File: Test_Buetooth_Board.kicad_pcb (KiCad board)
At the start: 2 copper layers, 100 x 100 mm, 7 parts, among them U1 WH-BLE103a, U2 YM23, U3 HLK-B40, U4 WL6601-TC, U5 E104-BT52, U6 E104-BT01, U7 E104-BT5010A

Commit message: SCH: Se termina la primera versión del sch. PCB: Se ordenan unos componentes
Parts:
- added C1: 100n, 1-Capacitor:C_0805_2012Metric, F.Cu at (130.5, 48.9)
- added C10: 10n, 1-Capacitor:C_0805_2012Metric, F.Cu at (172.6, 57.6)
- added C11: 100n, 1-Capacitor:C_0805_2012Metric, F.Cu at (234.1, 317.2)
- added C12: 10n, 1-Capacitor:C_0805_2012Metric, F.Cu at (234.1, 320.2)
- added C13: 100n, 1-Capacitor:C_0805_2012Metric, F.Cu at (153.2, 184.4)
- added C14: 10n, 1-Capacitor:C_0805_2012Metric, F.Cu at (153.2, 187.4)
- added C15: 100n, 1-Capacitor:C_0805_2012Metric, F.Cu at (153.2, 190.4)
- added C16: 100n, 1-Capacitor:C_0805_2012Metric, F.Cu at (153.2, 193.5)
- added C17: 10n, 1-Capacitor:C_0805_2012Metric, F.Cu at (157.6, 178.4)
- added C18: 100n, 1-Capacitor:C_0805_2012Metric, F.Cu at (157.6, 181.4)
- added C19: 100n, 1-Capacitor:C_0805_2012Metric, F.Cu at (157.6, 184.4)
- added C2: 100n, 1-Capacitor:C_0805_2012Metric, F.Cu at (121.1, 52.6)
- added C20: 10n, 1-Capacitor:C_0805_2012Metric, F.Cu at (157.6, 187.4)
- added C21: 100n, 1-Capacitor:C_0805_2012Metric, F.Cu at (157.6, 190.4)
- added C3: 10n, 1-Capacitor:C_0805_2012Metric, F.Cu at (123.2, 52.6)
- added C4: 100n, 1-Capacitor:C_0805_2012Metric, F.Cu at (103.5, 53.3)
- added C5: 100n, 1-Capacitor:C_0805_2012Metric, F.Cu at (160.4, 54.2)
- added C7: 100n, 1-Capacitor:C_0805_2012Metric, F.Cu at (136.1, 53.8)
- added C8: 10n, 1-Capacitor:C_0805_2012Metric, F.Cu at (138.1, 53.8)
- added C9: 100n, 1-Capacitor:C_0805_2012Metric, F.Cu at (174.7, 57.6)
- added D1: LED, 1-Led:LED_0805, F.Cu at (135.7, 70.2)
- added D2: LED, 1-Led:LED_0805, F.Cu at (127.8, 64.2)
- added D3: LED, 1-Led:LED_0805, F.Cu at (190.4, 65.5)
- added D4: LED, 1-Led:LED_0805, F.Cu at (161.5, 70.3)
- added D5: LED, 1-Led:LED_0805, F.Cu at (194.4, 65.5)
- added D6: LED, 1-Led:LED_0805, F.Cu at (159.2, 169.0)
- added D7: LED, 1-Led:LED_0805, F.Cu at (159.2, 172.0)
- added J1: Screw_Terminal_01x04, Connector_PinHeader_2.54mm:PinHeader_1x04_P2.54mm_Vertical, F.Cu at (101.5, 94.1)
- added J12: Screw_Terminal_01x02, Connector_PinHeader_2.54mm:PinHeader_1x02_P2.54mm_Vertical, F.Cu at (177.3, 77.9)
- added J13: Screw_Terminal_01x02, Connector_PinHeader_2.54mm:PinHeader_1x02_P2.54mm_Vertical, F.Cu at (181.9, 77.9)
- added J14: Screw_Terminal_01x02, Connector_PinHeader_2.54mm:PinHeader_1x02_P2.54mm_Vertical, F.Cu at (186.6, 77.9)
- added J15: Screw_Terminal_01x02, Connector_PinHeader_2.54mm:PinHeader_1x02_P2.54mm_Vertical, F.Cu at (230.7, 296.4)
- added J16: Screw_Terminal_01x05, Connector_PinHeader_2.54mm:PinHeader_1x05_P2.54mm_Vertical, F.Cu at (176.6, 72.3)
- added J17: Screw_Terminal_01x02, Connector_PinHeader_2.54mm:PinHeader_1x02_P2.54mm_Vertical, F.Cu at (202.8, 303.6)
- added J18: Screw_Terminal_01x02, Connector_PinHeader_2.54mm:PinHeader_1x02_P2.54mm_Vertical, F.Cu at (207.4, 303.6)
- added J19: Screw_Terminal_01x02, Connector_PinHeader_2.54mm:PinHeader_1x02_P2.54mm_Vertical, F.Cu at (212.1, 303.6)
- added J20: Screw_Terminal_01x02, Connector_PinHeader_2.54mm:PinHeader_1x02_P2.54mm_Vertical, F.Cu at (135.8, 164.8)
- added J21: Screw_Terminal_01x02, Connector_PinHeader_2.54mm:PinHeader_1x02_P2.54mm_Vertical, F.Cu at (140.5, 164.8)
- added J22: Screw_Terminal_01x02, Connector_PinHeader_2.54mm:PinHeader_1x02_P2.54mm_Vertical, F.Cu at (145.1, 164.8)
- added J23: Screw_Terminal_01x05, Connector_PinHeader_2.54mm:PinHeader_1x05_P2.54mm_Vertical, F.Cu at (153.5, 197.3)
- added J24: Screw_Terminal_01x02, Connector_PinHeader_2.54mm:PinHeader_1x02_P2.54mm_Vertical, F.Cu at (149.8, 164.8)
- added J25: Screw_Terminal_01x02, Connector_PinHeader_2.54mm:PinHeader_1x02_P2.54mm_Vertical, F.Cu at (121.9, 172.0)
- added J26: Screw_Terminal_01x02, Connector_PinHeader_2.54mm:PinHeader_1x02_P2.54mm_Vertical, F.Cu at (126.5, 172.0)
- added J27: Screw_Terminal_01x05, Connector_PinHeader_2.54mm:PinHeader_1x05_P2.54mm_Vertical, F.Cu at (158.1, 197.3)
- added J28: Screw_Terminal_01x06, Connector_PinHeader_2.54mm:PinHeader_1x06_P2.54mm_Vertical, F.Cu at (162.2, 179.2)
- added J29: Screw_Terminal_01x02, Connector_PinHeader_2.54mm:PinHeader_1x02_P2.54mm_Vertical, F.Cu at (131.2, 172.0)
- added J30: Screw_Terminal_01x02, Connector_PinHeader_2.54mm:PinHeader_1x02_P2.54mm_Vertical, F.Cu at (135.8, 172.0)
- added J31: Screw_Terminal_01x02, Connector_PinHeader_2.54mm:PinHeader_1x02_P2.54mm_Vertical, F.Cu at (140.5, 172.0)
- added J32: Screw_Terminal_01x07, 1-Pinhead:PinHeader_1x07_P2.54mm_Vertical, F.Cu at (154.4, 157.6)
- added J33: Screw_Terminal_01x06, Connector_PinHeader_2.54mm:PinHeader_1x06_P2.54mm_Vertical, F.Cu at (141.6, 72.2)
- added J34: Screw_Terminal_01x08, Connector_PinHeader_2.54mm:PinHeader_1x08_P2.54mm_Vertical, F.Cu at (103.5, 69.9)
- added J4: Screw_Terminal_01x02, Connector_PinHeader_2.54mm:PinHeader_1x02_P2.54mm_Vertical, F.Cu at (108.0, 79.0)
- added J5: Screw_Terminal_01x02, Connector_PinHeader_2.54mm:PinHeader_1x02_P2.54mm_Vertical, F.Cu at (112.7, 79.0)
- added J6: Screw_Terminal_01x02, Connector_PinHeader_2.54mm:PinHeader_1x02_P2.54mm_Vertical, F.Cu at (117.3, 79.0)
- added J7: Screw_Terminal_01x02, Connector_PinHeader_2.54mm:PinHeader_1x02_P2.54mm_Vertical, F.Cu at (143.2, 79.1)
- added J8: Screw_Terminal_01x02, Connector_PinHeader_2.54mm:PinHeader_1x02_P2.54mm_Vertical, F.Cu at (147.9, 79.1)
- added J9: Screw_Terminal_01x02, Connector_PinHeader_2.54mm:PinHeader_1x02_P2.54mm_Vertical, F.Cu at (152.6, 79.1)
- added Q1: MMBT3904, Package_TO_SOT_SMD:SOT-23, F.Cu at (127.9, 58.8)
- added Q2: MMBT3904, Package_TO_SOT_SMD:SOT-23, F.Cu at (135.7, 65.1)
- added Q3: MMBT3904, Package_TO_SOT_SMD:SOT-23, F.Cu at (161.6, 65.2)
- added Q4: MMBT3904, Package_TO_SOT_SMD:SOT-23, F.Cu at (190.4, 60.4)
- added Q5: MMBT3904, Package_TO_SOT_SMD:SOT-23, F.Cu at (194.5, 60.4)
- added Q6: MMBT3904, Package_TO_SOT_SMD:SOT-23, F.Cu at (144.1, 197.8)
- added Q7: MMBT3904, Package_TO_SOT_SMD:SOT-23, F.Cu at (144.1, 202.4)
- added R1: 100, 1-Resistor:R_0805_2012Metric, F.Cu at (100.0, 53.3)
- added R10: 10k, 1-Resistor:R_0805_2012Metric, F.Cu at (135.7, 62.1)
- added R11: 2k2, 1-Resistor:R_0805_2012Metric, F.Cu at (135.7, 68.2)
- added R12: 1k, 1-Resistor:R_0805_2012Metric, F.Cu at (161.6, 60.1)
- added R13: 10k, 1-Resistor:R_0805_2012Metric, F.Cu at (161.6, 62.1)
- added R15: 2k2, 1-Resistor:R_0805_2012Metric, F.Cu at (161.5, 68.2)
- added R16: 10k, 1-Resistor:R_0805_2012Metric, F.Cu at (169.9, 54.2)
- added R17: 10k, 1-Resistor:R_0805_2012Metric, F.Cu at (180.4, 62.1)
- added R18: 100, 1-Resistor:R_0805_2012Metric, F.Cu at (126.2, 187.2)
- added R19: 10k, 1-Resistor:R_0805_2012Metric, F.Cu at (182.6, 62.1)
- added R2: 100, 1-Resistor:R_0805_2012Metric, F.Cu at (130.5, 45.3)
- added R20: 1k, 1-Resistor:R_0805_2012Metric, F.Cu at (190.4, 55.4)
- added R21: 10k, 1-Resistor:R_0805_2012Metric, F.Cu at (190.4, 57.4)
- added R22: 2k2, 1-Resistor:R_0805_2012Metric, F.Cu at (190.4, 63.4)
- added R23: 1k, 1-Resistor:R_0805_2012Metric, F.Cu at (194.5, 55.4)
- added R24: 10k, 1-Resistor:R_0805_2012Metric, F.Cu at (194.5, 57.4)
- added R25: 2k2, 1-Resistor:R_0805_2012Metric, F.Cu at (194.5, 63.4)
- added R26: 10k, 1-Resistor:R_0805_2012Metric, F.Cu at (130.6, 187.2)
- added R27: 10k, 1-Resistor:R_0805_2012Metric, F.Cu at (130.6, 190.2)
- added R28: 1k, 1-Resistor:R_0805_2012Metric, F.Cu at (130.6, 193.1)
- added R29: 10k, 1-Resistor:R_0805_2012Metric, F.Cu at (130.6, 196.1)
- added R3: 1k, 1-Resistor:R_0805_2012Metric, F.Cu at (127.9, 53.6)
- added R30: 2k2, 1-Resistor:R_0805_2012Metric, F.Cu at (130.6, 199.0)
- added R31: 10k, 1-Resistor:R_0805_2012Metric, F.Cu at (135.0, 178.4)
- added R32: 10k, 1-Resistor:R_0805_2012Metric, F.Cu at (135.0, 181.3)
- added R33: 10k, 1-Resistor:R_0805_2012Metric, F.Cu at (135.0, 184.3)
- added R34: 1k, 1-Resistor:R_0805_2012Metric, F.Cu at (135.0, 187.2)
- added R35: 10k, 1-Resistor:R_0805_2012Metric, F.Cu at (135.0, 190.2)
- added R36: 2k2, 1-Resistor:R_0805_2012Metric, F.Cu at (135.0, 193.1)
- added R37: 100, 1-Resistor:R_0805_2012Metric, F.Cu at (135.0, 196.1)
- added R38: 10k, 1-Resistor:R_0805_2012Metric, F.Cu at (135.0, 199.0)
- added R39: 10k, 1-Resistor:R_0805_2012Metric, F.Cu at (139.4, 178.4)
- added R4: 2k2, 1-Resistor:R_0805_2012Metric, F.Cu at (127.8, 62.0)
- added R40: 10k, 1-Resistor:R_0805_2012Metric, F.Cu at (139.4, 181.3)
- added R41: 100, 1-Resistor:R_0805_2012Metric, F.Cu at (139.4, 184.3)
- added R42: 10k, 1-Resistor:R_0805_2012Metric, F.Cu at (139.4, 187.2)
- added R43: 10k, 1-Resistor:R_0805_2012Metric, F.Cu at (139.4, 190.2)
- added R5: 10k, 1-Resistor:R_0805_2012Metric, F.Cu at (127.9, 55.6)
- added R6: 1k, 1-Resistor:R_0805_2012Metric, F.Cu at (106.8, 55.8)
- added R7: 100, 1-Resistor:R_0805_2012Metric, F.Cu at (163.9, 54.2)
- added R8: 10K, 1-Resistor:R_0805_2012Metric, F.Cu at (160.4, 56.6)
- added R9: 1k, 1-Resistor:R_0805_2012Metric, F.Cu at (135.8, 60.1)
- added S1: 10-XX, 1-Switch:SW_PUSH_6mm_H7.3mm, F.Cu at (101.8, 58.9)
- added S2: 10-XX, 1-Switch:SW_PUSH_6mm_H7.3mm, F.Cu at (124.8, 47.1)
- added S3: 10-XX, 1-Switch:SW_PUSH_6mm_H7.3mm, F.Cu at (162.2, 48.6)
- added S5: 10-XX, 1-Switch:SW_PUSH_6mm_H7.3mm, F.Cu at (171.7, 48.6)
- added S6: 10-XX, 1-Switch:SW_PUSH_6mm_H7.3mm, F.Cu at (114.6, 183.1)
- added S7: 10-XX, 1-Switch:SW_PUSH_6mm_H7.3mm, F.Cu at (114.6, 191.1)
- added S8: 10-XX, 1-Switch:SW_PUSH_6mm_H7.3mm, F.Cu at (114.6, 199.0)
- moved U4 363.1 mm to (207.6, 285.0)
- moved U6 301.0 mm to (219.8, 147.7)
- moved U5 301.0 mm to (223.2, 213.0)
- moved U7 301.0 mm to (222.1, 177.4)
- moved U3 164.1 mm to (181.7, 51.1), turned to 0 degrees
- moved U2 163.1 mm to (148.2, 54.7), turned to 0 degrees
- moved U1 104.9 mm to (113.9, 52.5), turned to 0 degrees
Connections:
- U1 pad 1: unconnected-(U1-nReload-Pad1) -> RELOAD_1
- U1 pad 10: unconnected-(U1-UART_RX-Pad10) -> RX1
- U1 pad 11: unconnected-(U1-LINK-Pad11) -> LINK
- U1 pad 12: unconnected-(U1-nRESET-Pad12) -> RST_1
- U1 pad 13: unconnected-(U1-GND-Pad13) -> GND
- U1 pad 14: unconnected-(U1-VBAT-Pad14) -> VCC1
- U1 pad 15: unconnected-(U1-GND-Pad15) -> GND
- U1 pad 17: unconnected-(U1-GPIO3-Pad17) -> GPIO3_1
- U1 pad 2: unconnected-(U1-Wake-Pad2) -> WAKEUP_1
- U1 pad 3: unconnected-(U1-GPIO1-Pad3) -> Net-(U1-GPIO1)
- U1 pad 4: unconnected-(U1-ADC-Pad4) -> ADC_1
- U1 pad 5: unconnected-(U1-GPIO2-Pad5) -> GPIO2_1
- U1 pad 6: unconnected-(U1-VBAT-Pad6) -> VCC1
- U1 pad 7: unconnected-(U1-SWCLK-Pad7) -> SWCLK_1
- U1 pad 8: unconnected-(U1-SWDIO-Pad8) -> SWDIO_1
- U1 pad 9: unconnected-(U1-UART_TX-Pad9) -> TX1
- U2 pad 1: unconnected-(U2-VCC-Pad1) -> VCC2
- U2 pad 16: unconnected-(U2-EINT2-Pad16) -> EINT2_2
- U2 pad 17: unconnected-(U2-ALED-Pad17) -> ALED
- U2 pad 19: unconnected-(U2-TXD-Pad19) -> TX2
- U2 pad 20: unconnected-(U2-RXD-Pad20) -> RX2
- U2 pad 21: unconnected-(U2-EINT1-Pad21) -> EINT1_2
- U2 pad 22: unconnected-(U2-PWRC-Pad22) -> PWRC
- U2 pad 23: unconnected-(U2-RST-Pad23) -> RST_2
- U2 pad 24: unconnected-(U2-GND-Pad24) -> GND
- U2 pad 4: unconnected-(U2-OUTPUT1-Pad4) -> OUTPUT1_2
- U2 pad 5: unconnected-(U2-OUTPUT2-Pad5) -> OUTPUT2_2
- U2 pad 6: unconnected-(U2-STATUS-Pad6) -> STATUS
- U3 pad 1: unconnected-(U3-GND-Pad1) -> GND
- U3 pad 10: unconnected-(U3-GND-Pad10) -> GND
- U3 pad 16: unconnected-(U3-PC7-Pad16) -> PC7_SLEEP_OUTPUT
- U3 pad 17: unconnected-(U3-PC6-Pad17) -> PC6_SLEEP_INPUT
- U3 pad 18: unconnected-(U3-PC5-Pad18) -> PC5_KEY_INPUT
- U3 pad 23: unconnected-(U3-TXD-Pad23) -> TX3
- U3 pad 24: unconnected-(U3-RXD-Pad24) -> RX3
- U3 pad 25: unconnected-(U3-PA4-Pad25) -> PA4_CONNECTED_OUTPUT
- U3 pad 26: unconnected-(U3-PA5-Pad26) -> PA4_MODE_OUTPUT
- U3 pad 28: unconnected-(U3-GND-Pad28) -> GND
- U3 pad 7: unconnected-(U3-RESET-Pad7) -> RST_3
- U3 pad 9: unconnected-(U3-VBAT-Pad9) -> VCC3
- U4 pad 1: unconnected-(U4-VDD-Pad1) -> VCC4
- U4 pad 2: unconnected-(U4-GND-Pad2) -> GND
- U4 pad 3: unconnected-(U4-TX-Pad3) -> TX4
- U4 pad 4: unconnected-(U4-RX-Pad4) -> RX4
- U4 pad 5: unconnected-(U4-IO1-Pad5) -> IO1
- U4 pad 6: unconnected-(U4-IO2-Pad6) -> IO2
- U5 pad 1: unconnected-(U5-GND-Pad1) -> GND
- U5 pad 10: unconnected-(U5-CLK-Pad10) -> SWCLK_5
- U5 pad 12: unconnected-(U5-GND-Pad12) -> GND
- U5 pad 13: unconnected-(U5-WKP-Pad13) -> WKP_5
- U5 pad 14: unconnected-(U5-TXD-Pad14) -> TX5
- U5 pad 15: unconnected-(U5-RXD-Pad15) -> RX5
- U5 pad 16: unconnected-(U5-LINK-Pad16) -> LINK_5
- U5 pad 17: unconnected-(U5-DATA-Pad17) -> DATA_5
- U5 pad 18: unconnected-(U5-GND-Pad18) -> GND
- U5 pad 3: unconnected-(U5-VCC-Pad3) -> VCC5
- U5 pad 4: unconnected-(U5-VH+-Pad4) -> VCC5
- U5 pad 5: unconnected-(U5-GND-Pad5) -> GND
- U5 pad 6: unconnected-(U5-GND-Pad6) -> GND
- U5 pad 7: unconnected-(U5-RST-Pad7) -> RST_5
- U5 pad 8: unconnected-(U5-SWDIO-Pad8) -> SWDIO_5
- U6 pad 1: unconnected-(U6-GND-Pad1) -> GND
- U6 pad 10: unconnected-(U6-P1.5_LINK-Pad10) -> LINK_6
- U6 pad 11: unconnected-(U6-P1.4_DATA-Pad11) -> DATA_6
- U6 pad 13: unconnected-(U6-P1.2_WKP-Pad13) -> WKP_6
- U6 pad 16: unconnected-(U6-P0.7_AT-Pad16) -> P0.7
- U6 pad 17: unconnected-(U6-P0.6_AT-Pad17) -> P0.6
- U6 pad 18: unconnected-(U6-P0.5_DISC-Pad18) -> DISC_6
- U6 pad 2: unconnected-(U6-VCC-Pad2) -> VCC6
- U6 pad 20: unconnected-(U6-P0.3_TXD-Pad20) -> TX6
- U6 pad 21: unconnected-(U6-P0.2_RXD-Pad21) -> RX6
- U6 pad 22: unconnected-(U6-P0.1_AT-Pad22) -> P0.1
- U6 pad 23: unconnected-(U6-P0.0_AT-Pad23) -> P0.0
- U6 pad 24: unconnected-(U6-RESET-Pad24) -> RST_6
- U6 pad 5: unconnected-(U6-P2.0_MODE-Pad5) -> MODE_6
- U6 pad 8: unconnected-(U6-SCL-Pad8) -> SCL_6
- U6 pad 9: unconnected-(U6-SDA-Pad9) -> SDA_6
- U7 pad 1: unconnected-(U7-GND-Pad1) -> GND
- U7 pad 16: unconnected-(U7-GND-Pad16) -> GND
- U7 pad 17: unconnected-(U7-VCC-Pad17) -> VCC7
- U7 pad 18: unconnected-(U7-RXD-Pad18) -> RX7
- U7 pad 19: unconnected-(U7-TXD-Pad19) -> TX7
- U7 pad 20: unconnected-(U7-RTS-Pad20) -> RTS_7
- U7 pad 21: unconnected-(U7-CTS-Pad21) -> CTS_7
- U7 pad 22: unconnected-(U7-RST-Pad22) -> RST_7
- U7 pad 4: unconnected-(U7-MOD-Pad4) -> MOD_7
- U7 pad 5: unconnected-(U7-WKP-Pad5) -> WKP_7
- U7 pad 6: unconnected-(U7-DISC-Pad6) -> DISC_7
- U7 pad 7: unconnected-(U7-LINK-Pad7) -> LINK_7
- U7 pad 8: unconnected-(U7-DATA-Pad8) -> DATA_7
- U7 pad 9: unconnected-(U7-GND-Pad9) -> GND
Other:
- outline, holes or cut-outs redrawn

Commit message: Acance del PCB, se acomoda la mayoría de componentes
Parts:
- moved C12 237.9 mm to (172.5, 90.4), turned to -90 degrees
- moved C11 235.5 mm to (170.4, 90.4), turned to -90 degrees
- moved J17 216.0 mm to (163.7, 91.2), turned to -90 degrees
- moved J18 212.3 mm to (163.7, 95.8), turned to -90 degrees
- moved J15 210.6 mm to (169.4, 94.8)
- moved J19 208.8 mm to (163.7, 100.5), turned to -90 degrees
- moved U4 191.8 mm to (185.5, 94.4), turned to -90 degrees
- moved U5 131.5 mm to (117.0, 135.4)
- moved S8 104.9 mm to (193.8, 130.2), turned to -90 degrees
- moved R43 88.1 mm to (195.7, 122.4)
- moved J27 85.1 mm to (163.5, 112.4), turned to -90 degrees
- moved C15 83.0 mm to (105.9, 122.3)
- moved J23 80.6 mm to (121.9, 123.2), turned to -90 degrees
- moved R41 79.6 mm to (192.0, 124.5)
- moved Q7 78.8 mm to (166.4, 126.9), turned to -90 degrees
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
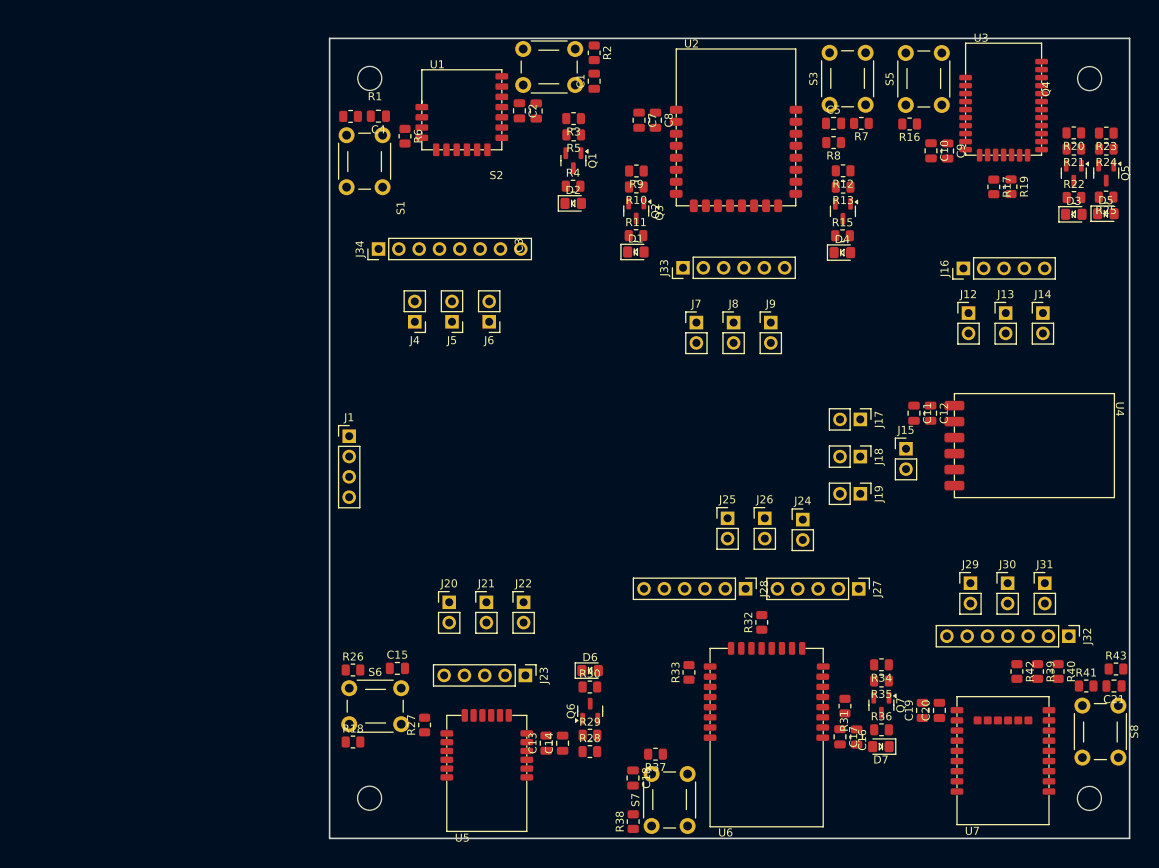
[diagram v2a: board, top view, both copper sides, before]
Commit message: Se acaba de colocar un header por cada placa para probar en otra próxima rama la utilidad, en main seguiremos con el planteamiento inicial de utiizar jumpers
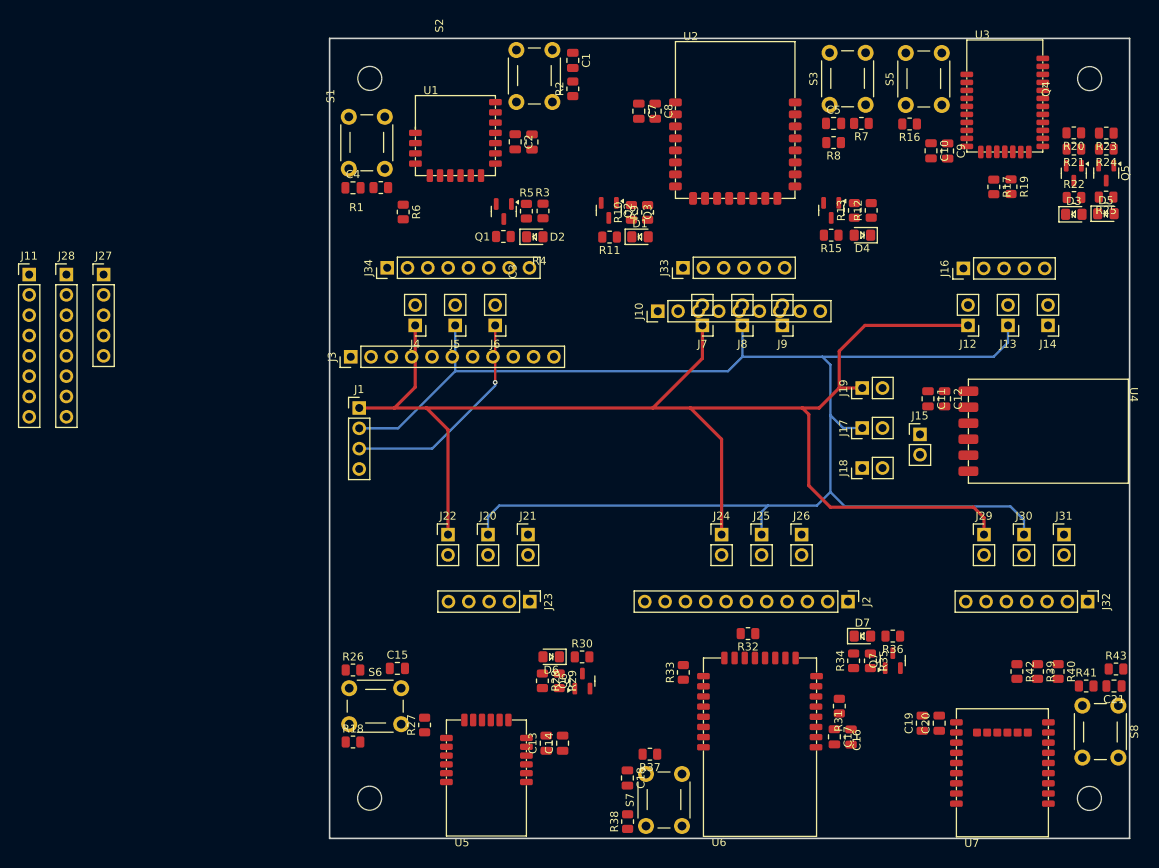
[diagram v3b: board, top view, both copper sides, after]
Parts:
- added J10: Screw_Terminal_01x09, Connector_PinHeader_2.54mm:PinHeader_1x09_P2.54mm_Vertical, F.Cu at (138.4, 77.6)
- added J11: Screw_Terminal_01x08, Connector_PinHeader_2.54mm:PinHeader_1x08_P2.54mm_Vertical, F.Cu at (59.9, 73.1)
- added J2: Screw_Terminal_01x11, Connector_PinHeader_2.54mm:PinHeader_1x11_P2.54mm_Vertical, F.Cu at (162.2, 113.9)
- added J3: Screw_Terminal_01x11, Connector_PinHeader_2.54mm:PinHeader_1x11_P2.54mm_Vertical, F.Cu at (100.0, 83.3)
- J28: value Screw_Terminal_01x06 -> Screw_Terminal_01x08; footprint Connector_PinHeader_2.54mm:PinHeader_1x06_P2.54mm_Vertical -> Connector_PinHeader_2.54mm:PinHeader_1x08_P2.54mm_Vertical
- moved J27 102.2 mm to (69.2, 73.1), turned to 0 degrees
- moved J28 93.5 mm to (64.5, 73.1), turned to 0 degrees
- moved D7 14.0 mm to (164.0, 118.3), turned to 0 degrees
- moved J19 13.2 mm to (164.0, 87.2), turned to 90 degrees
- moved J22 12.7 mm to (112.2, 105.6)
- moved R3 12.2 mm to (124.1, 65.1), turned to 90 degrees
- moved R36 11.8 mm to (167.8, 118.3), turned to 180 degrees
- moved R5 11.2 mm to (122.0, 65.1), turned to 90 degrees
- moved Q1 10.8 mm to (119.2, 65.2)
- moved R4 10.7 mm to (119.1, 68.3), turned to 180 degrees
- moved R28 10.7 mm to (124.0, 123.8), turned to -90 degrees
- moved J24 10.3 mm to (146.4, 105.6)
- moved J21 9.93 mm to (122.2, 105.6)
- moved J20 9.75 mm to (117.2, 105.6)
- moved R1 9.67 mm to (103.8, 62.2), turned to 180 degrees
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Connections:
- J27 pad 1: MODE_6 -> VCC4
- J27 pad 2: SCL_6 -> TX4
- J27 pad 3: SDA_6 -> RX4
- J27 pad 4: LINK_6 -> IO1
- J27 pad 5: DATA_6 -> IO2
- J28 pad 1: WKP_6 -> VCC5
- J28 pad 2: P0.7 -> SWDIO_5
- J28 pad 3: P0.6 -> SWCLK_5
- J28 pad 4: DISC_6 -> WKP_5
- J28 pad 5: P0.1 -> TX5
- J28 pad 6: P0.0 -> RX5
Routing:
- net TX: track 0.00 -> 197.0 mm
- net +3.3V: track 0.00 -> 180.3 mm
- net RX: track 0.00 -> 27.8 mm, vias 0 -> 1

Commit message: SCH: Se modificaron VCC que no estaban en el orden correcto, re remplaza la librería del pulsador, se areglan otros errores, tener en cuenta para la otra rama o eliminarla. PCB: Ruteado, falta terminar GND y revisar conexiones
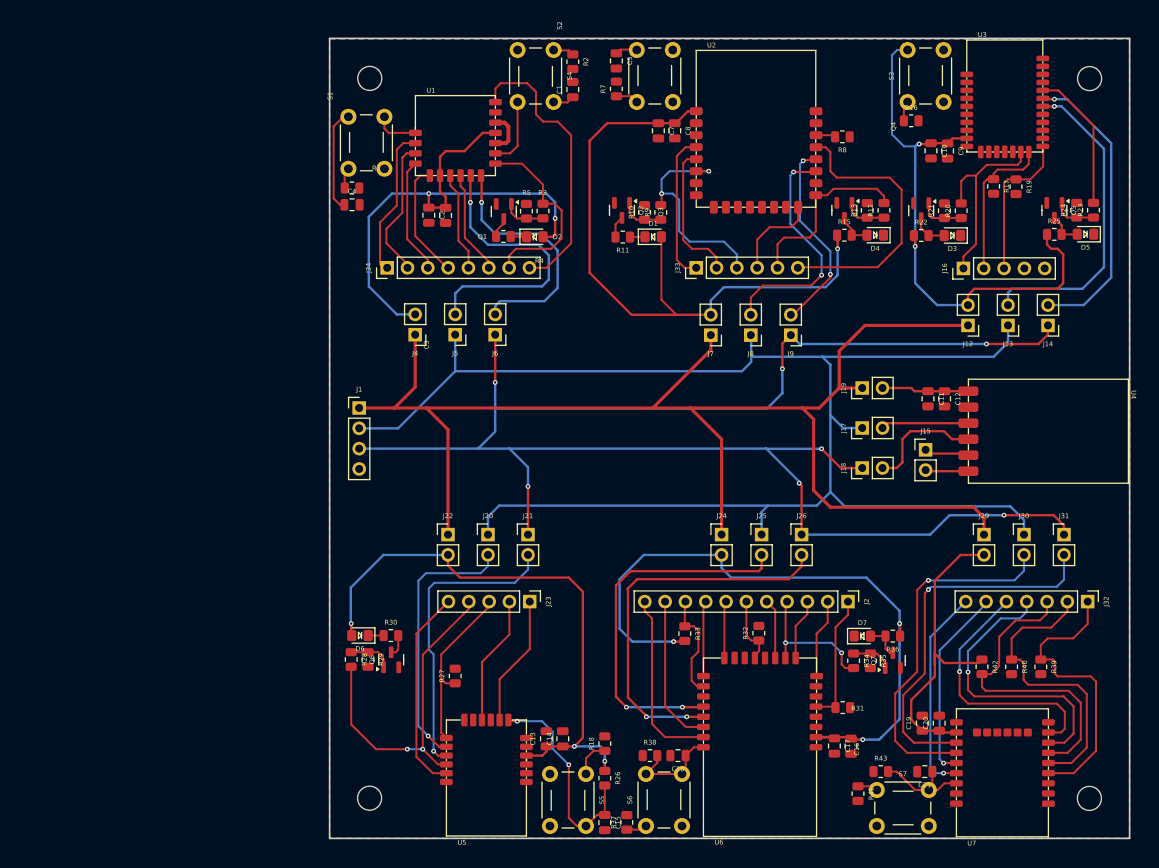
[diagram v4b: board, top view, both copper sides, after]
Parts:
- removed J10: Screw_Terminal_01x09, Connector_PinHeader_2.54mm:PinHeader_1x09_P2.54mm_Vertical
- removed J11, J28: Screw_Terminal_01x08, Connector_PinHeader_2.54mm:PinHeader_1x08_P2.54mm_Vertical
- removed J27: Screw_Terminal_01x05, Connector_PinHeader_2.54mm:PinHeader_1x05_P2.54mm_Vertical
- removed J3: Screw_Terminal_01x11, Connector_PinHeader_2.54mm:PinHeader_1x11_P2.54mm_Vertical
- removed R6: 1k, 1-Resistor:R_0805_2012Metric
- removed S8: 10-XX, 1-Switch:SW_PUSH_6mm_H7.3mm
- added S4: SW_PUSH_6mm_H7.3mm, 1-Switch:SW_PUSH_6mm_H7.3mm, F.Cu at (123.2, 48.2)
- S1, S2, S3, S5, S6, S7: value 10-XX -> SW_PUSH_6mm_H7.3mm
- moved S5 100.5 mm to (127.2, 138.7), turned to -90 degrees
- moved S6 38.0 mm to (139.2, 138.7), turned to 90 degrees
- moved R26 34.3 mm to (131.8, 136.0), turned to -90 degrees
- moved C15 32.3 mm to (131.8, 141.6), turned to -90 degrees
- moved R43 32.1 mm to (166.3, 135.2)
- moved R41 31.5 mm to (163.4, 137.9), turned to -90 degrees
- moved R18 31.5 mm to (131.8, 131.7), turned to 90 degrees
- moved R7 30.9 mm to (133.2, 49.9), turned to 90 degrees
- moved S7 29.9 mm to (169.1, 139.7), turned to 0 degrees
- moved C5 28.3 mm to (133.2, 46.4), turned to -90 degrees
- moved C21 26.0 mm to (171.8, 135.2)
- moved Q6 24.0 mm to (105.1, 121.2)
- moved R28 24.0 mm to (100.1, 121.2)
- moved R30 24.0 mm to (105.1, 118.2)
- moved D6 24.0 mm to (101.2, 118.2)
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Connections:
- R1 pad 1: Net-(S1-P) -> Net-(R1-Pad1)
- R18 pad 1: Net-(S6-P) -> Net-(R18-Pad1)
- R2 pad 1: Net-(S2-P) -> Net-(R2-Pad1)
- R37 pad 1: Net-(S7-P) -> Net-(R37-Pad1)
- R38 pad 1: VCC5 -> VCC6
- R41 pad 1: Net-(S8-P) -> Net-(R41-Pad1)
- R42 pad 1: VCC6 -> VCC7
- R43 pad 1: VCC5 -> VCC7
- R7 pad 1: Net-(S3-P) -> Net-(R7-Pad1)
- S1 pad 1: RELOAD_1 -> Net-(R1-Pad1)
- S1 pad 2: unconnected-(S1-S1-Pad2) -> RELOAD_1
- S1 pad 3: Net-(S1-P) -> Net-(R1-Pad1)
- S1 pad 4: unconnected-(S1-P1-Pad4) -> RELOAD_1
- S2 pad 1: RST_1 -> Net-(R7-Pad1)
- S2 pad 2: unconnected-(S2-S1-Pad2) -> RST_2
- S2 pad 3: Net-(S2-P) -> Net-(R7-Pad1)
- S2 pad 4: unconnected-(S2-P1-Pad4) -> RST_2
- S3 pad 1: RST_2 -> RST_3
- S3 pad 2: unconnected-(S3-S1-Pad2) -> VCC3
- S3 pad 3: Net-(S3-P) -> RST_3
- S3 pad 4: unconnected-(S3-P1-Pad4) -> VCC3
- S5 pad 1: VCC3 -> Net-(R18-Pad1)
- S5 pad 2: unconnected-(S5-S1-Pad2) -> RST_5
- S5 pad 3: RST_3 -> Net-(R18-Pad1)
- S5 pad 4: unconnected-(S5-P1-Pad4) -> RST_5
- S6 pad 1: RST_5 -> Net-(R37-Pad1)
- S6 pad 2: unconnected-(S6-S1-Pad2) -> RST_6
- S6 pad 3: Net-(S6-P) -> Net-(R37-Pad1)
- S6 pad 4: unconnected-(S6-P1-Pad4) -> RST_6
- S7 pad 1: RST_6 -> Net-(R41-Pad1)
- S7 pad 2: unconnected-(S7-S1-Pad2) -> RST_7
- S7 pad 3: Net-(S7-P) -> Net-(R41-Pad1)
- S7 pad 4: unconnected-(S7-P1-Pad4) -> RST_7
- U1 pad 3: Net-(U1-GPIO1) -> GPIO1_1
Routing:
- net RX: track 27.8 -> 217.5 mm, vias 1 -> 7
- net VCC6: track 0.00 -> 84.3 mm, vias 0 -> 3
- net VCC2: track 0.00 -> 83.2 mm, vias 0 -> 1
- net VCC5: track 0.00 -> 73.9 mm, vias 0 -> 3
- net VCC3: track 0.00 -> 70.0 mm, vias 0 -> 2
- net VCC1: track 0.00 -> 65.5 mm, vias 0 -> 2
- net RX6: track 0.00 -> 48.4 mm, vias 0 -> 2
- net RX7: track 0.00 -> 46.9 mm, vias 0 -> 1
- net TX6: track 0.00 -> 46.2 mm, vias 0 -> 2
- net TX7: track 0.00 -> 44.6 mm, vias 0 -> 1
- net LINK_5: track 0.00 -> 42.0 mm, vias 0 -> 2
- net VCC7: track 0.00 -> 40.3 mm
- net TX3: track 0.00 -> 39.5 mm, vias 0 -> 1
- net DISC_7: track 0.00 -> 39.0 mm
- net RX5: track 0.00 -> 37.6 mm, vias 0 -> 1
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- added copper zone on B.Cu, net GND
- added copper zone on F.Cu, net GND
